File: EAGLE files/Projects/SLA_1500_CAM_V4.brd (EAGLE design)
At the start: 37.8 x 26.4 mm, 88 parts, among them J2 JST GH SM06B, J3 MOLEX 53261-03, J4 MOLEX 53261-04, J5 MOLEX 53261-04, J6 MOLEX 53261-04, U11 TXS0102, U2 TPS73633DCQR, U8 TXS0102, U9 TXS0102

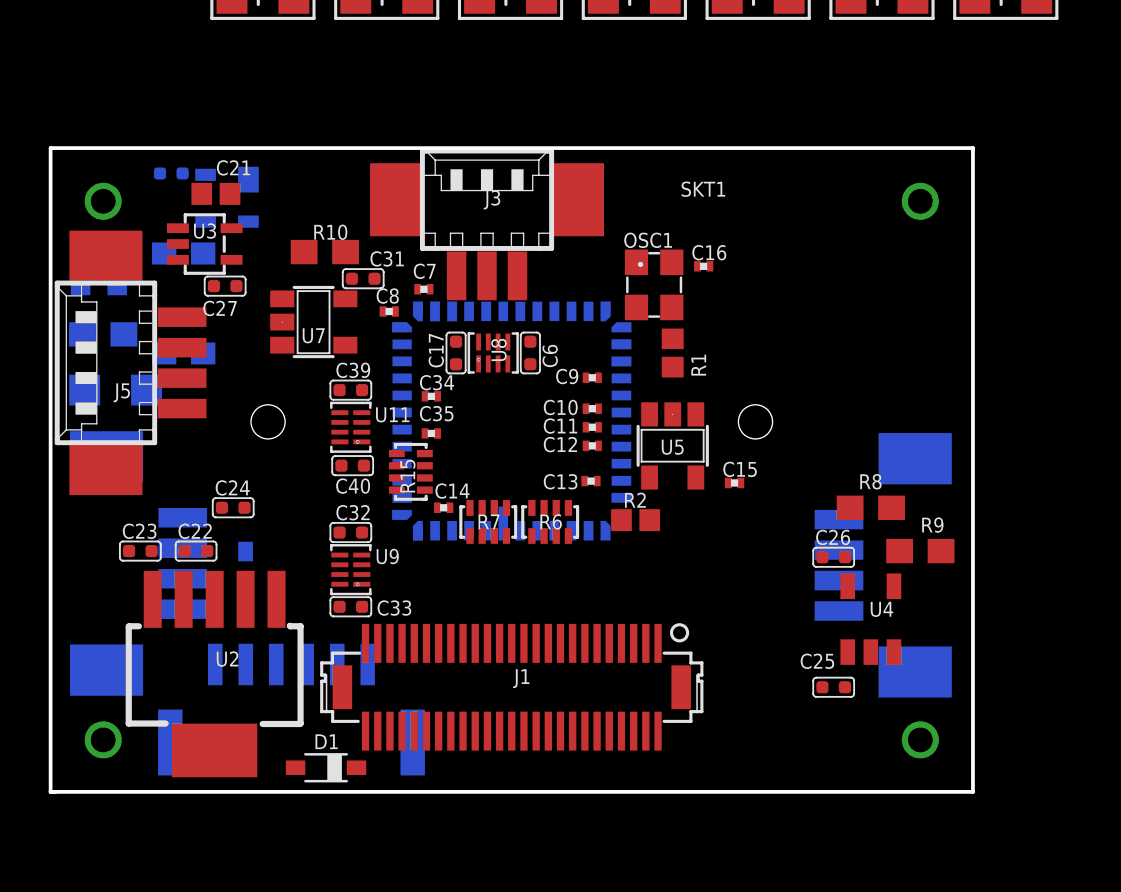
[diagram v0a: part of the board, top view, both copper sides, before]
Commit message: Update SLA1500 CAM V4
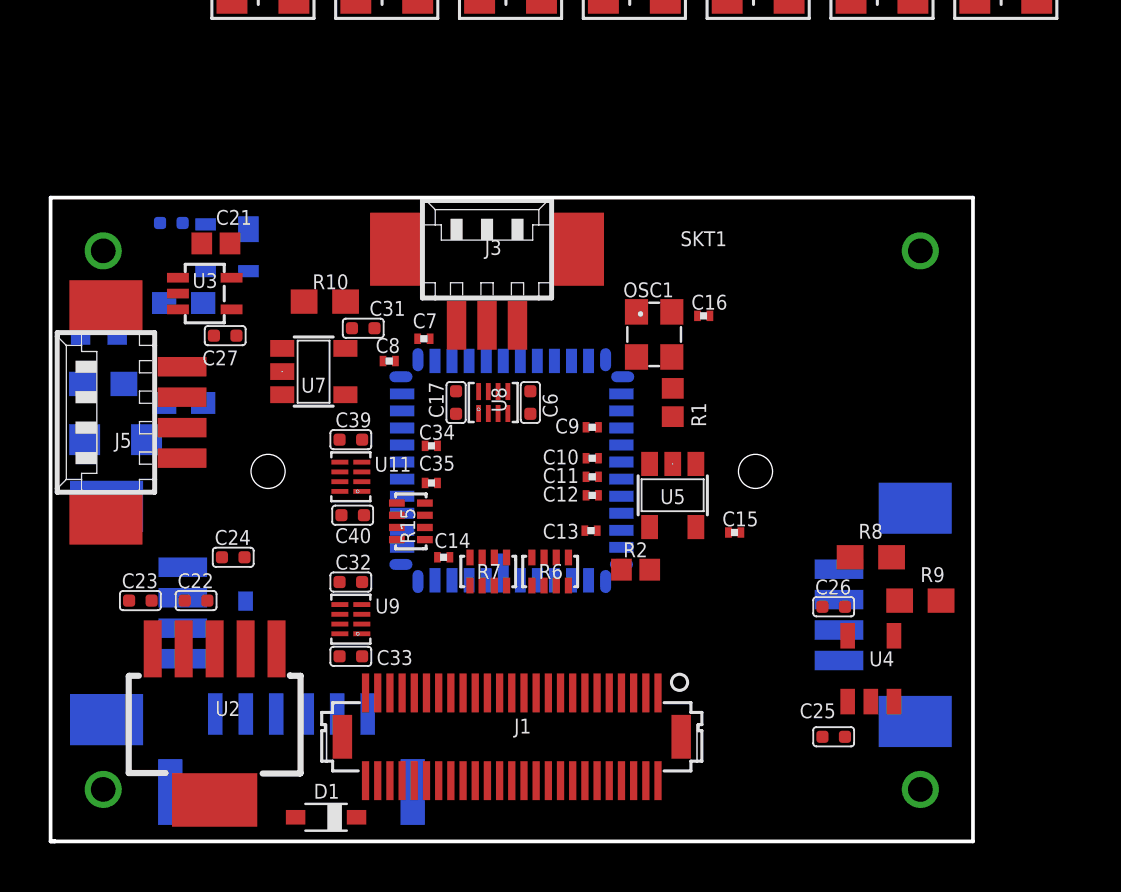
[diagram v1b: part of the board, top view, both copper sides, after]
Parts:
- U1: device Sightline:ILCC48 -> Sightline:ILCC48_KD
- moved R10 2.03 mm to (-7.67, 6.93)
- moved C10 2.03 mm to (3.30, 0.51)
- moved C11 2.03 mm to (3.30, -0.25)
- moved C12 2.03 mm to (3.30, -1.02)
- moved C13 2.03 mm to (3.25, -2.46)
- moved C14 2.03 mm to (-2.79, -3.56)
- moved C15 2.03 mm to (9.14, -2.54)
- moved C16 2.03 mm to (7.87, 6.35)
- moved C21 2.03 mm to (-12.1, 9.32)
- moved C24 2.03 mm to (-11.4, -3.56)
- moved C25 2.03 mm to (13.2, -10.9)
- moved C26 2.03 mm to (13.2, -5.59)
- moved C27 2.03 mm to (-11.8, 5.54)
- moved C30 2.03 mm to (-14.0, 10.2)
- moved C31 2.03 mm to (-6.10, 5.84)
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
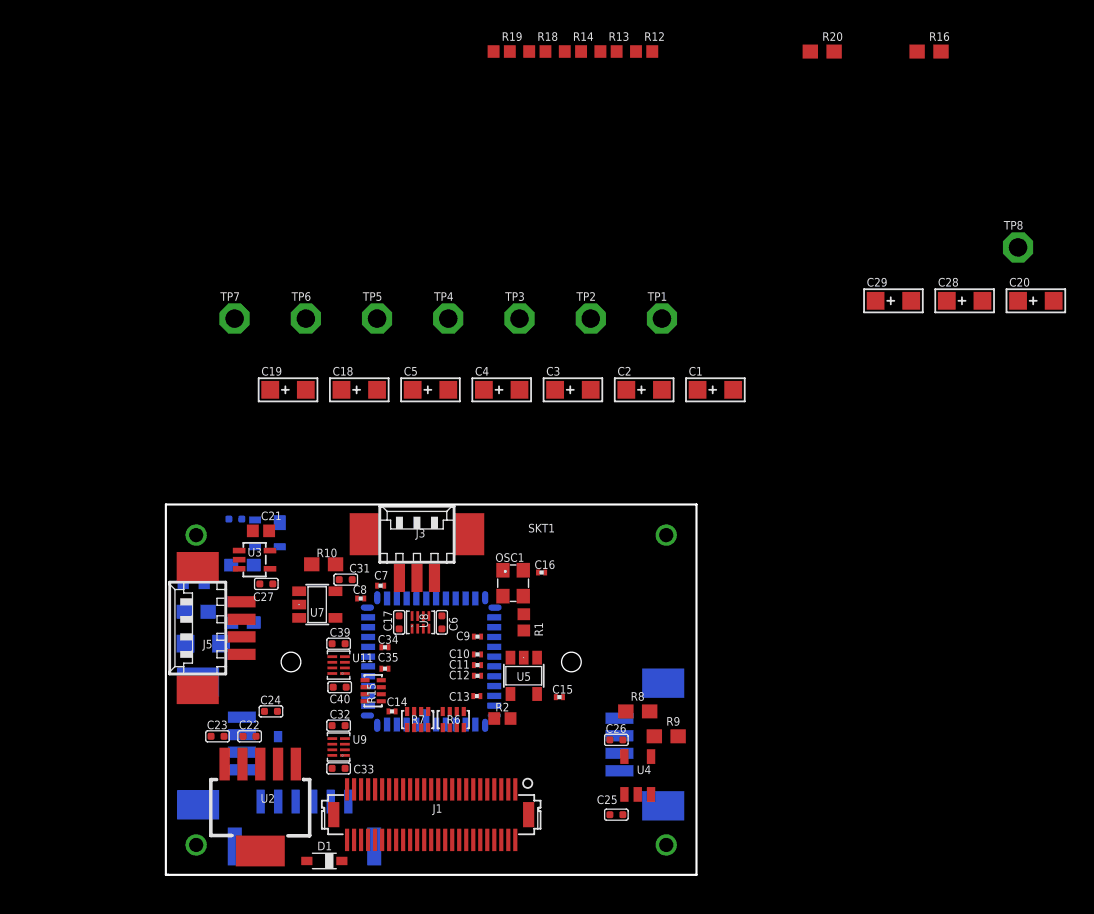
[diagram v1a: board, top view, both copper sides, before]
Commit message: Update SLA1500 CAM V4
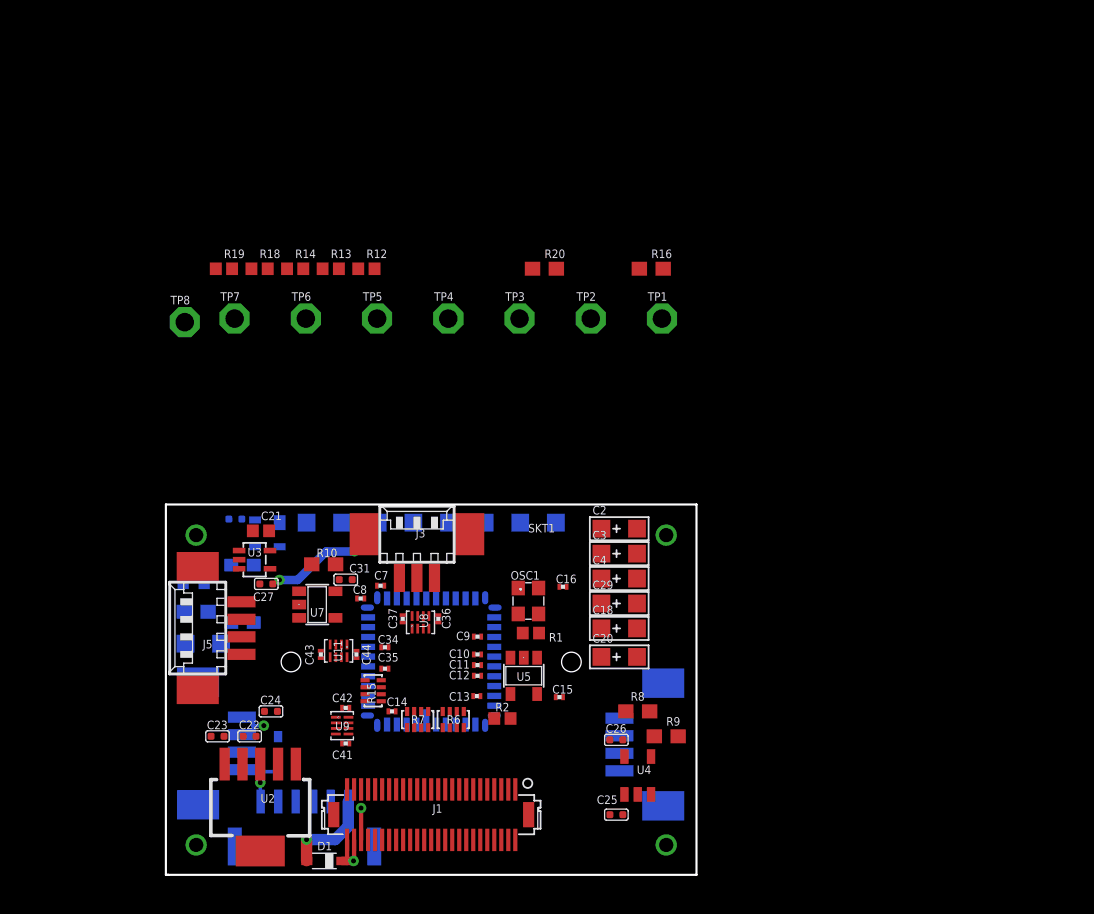
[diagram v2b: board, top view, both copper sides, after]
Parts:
- removed C17, C32, C33, C39, C40, C6: 100nf, Seeed-Capacitor:C0402
- added C36, C37, C41, C42, C43, C44: (no value), Sightline:R0201
- moved TP8 59.7 mm to (-17.6, 24.2)
- moved C28 43.6 mm to (-2.54, 9.91), flipped to the bottom, turned to 180 degrees
- moved C20 39.1 mm to (13.4, 0.33)
- moved C1 29.5 mm to (-7.62, 9.91), flipped to the bottom
- moved C29 29.1 mm to (13.4, 4.14)
- moved C18 25.2 mm to (13.4, 2.36)
- moved R13 25.2 mm to (-7.16, 28.0)
- moved R18 25.2 mm to (-12.2, 28.0)
- moved R19 25.2 mm to (-14.8, 28.0)
- moved R12 25.2 mm to (-4.62, 28.0)
- moved R14 25.2 mm to (-9.70, 28.0)
- moved R16 25.2 mm to (15.7, 28.0)
- moved R20 25.2 mm to (8.08, 28.0)
- moved C19 15.9 mm to (2.54, 9.91), flipped to the bottom
- moved C4 15.9 mm to (13.4, 5.92)
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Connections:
- net GND: now also C36.2, C37.2, C41.2, C42.2, C43.2, C44.2; no longer C17.2, C32.1, C33.2, C39.1, C40.2, C6.1
- net P1P8V: now also C36.1, C41.1, C43.1; no longer C32.2, C39.2, C6.2
- net P3P3V: now also C37.1, C42.1, C44.1; no longer C17.1, C33.1, C40.1
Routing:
- net N$34: track 0.00 -> 6.67 mm, vias 0 -> 1
- net N$2: track 0.00 -> 6.21 mm, vias 0 -> 2
- net N$39: track 0.00 -> 5.47 mm
- net GND: track 0.00 -> 4.94 mm, vias 0 -> 2
- net P5V: track 0.00 -> 3.85 mm, vias 0 -> 1
- net P1P8V: track 0.00 -> 2.27 mm, vias 0 -> 1
- added copper zone on layer 15, net GND
- added copper zone on layer 2, net P1P8V
- added copper zone on layer 2, net P2P8V
- added copper zone on layer 2, net P3P3V
- added copper zone on layer 2, net P5V

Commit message: Update SLA1500 CAM
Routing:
- net P5V: track 3.85 -> 2.87 mm
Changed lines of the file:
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@@
 </polygon>
 <wire x1="-12.7" y1="-5.217" x2="-13.502" y2="-5.217" width="0.254" layer="16"/>
-<wire x1="-12.164" y1="-9.988" x2="-12.192" y2="-9.988" width="0.254" layer="16"/>
-<wire x1="-12.192" y1="-9.988" x2="-12.192" y2="-8.636" width="0.254" layer="16"/>
-<via x="-12.192" y="-8.636" extent="15-16" drill="0.35"/>
+<wire x1="-12.164" y1="-9.988" x2="-12.1666" y2="-9.988" width="0.254" layer="16"/>
+<wire x1="-12.1666" y1="-9.988" x2="-12.1666" y2="-8.5344" width="0.254" layer="16"/>
+<via x="-12.1666" y="-8.5344" extent="15-16" drill="0.35"/>
 <wire x1="-13.502" y1="-3.967" x2="-12.797" y2="-3.967" width="0.254" layer="16"/>
 <wire x1="-12.797" y1="-3.967" x2="-12.7" y2="-4.064" width="0.254" layer="16"/>
@@
 <wire x1="-11.8925" y1="-3.556" x2="-12.7" y2="-4.064" width="0" layer="19" extent="1-16"/>
 <wire x1="-14.7775" y1="-5.334" x2="-13.502" y2="-5.217" width="0" layer="19" extent="1-16"/>
-<wire x1="-12.192" y1="-7.314" x2="-12.192" y2="-8.636" width="0" layer="19" extent="1-16"/>
+<wire x1="-12.192" y1="-7.314" x2="-12.1666" y2="-8.5344" width="0" layer="19" extent="1-16"/>
 <wire x1="14.6812" y1="9.4742" x2="16.764" y2="9.017" width="0" layer="19" extent="1-1"/>
 <wire x1="14.6812" y1="7.6962" x2="14.6812" y2="9.4742" width="0" layer="19" extent="1-1"/>
@@
 <vertex x="-19.0754" y="6.096"/>
 </polygon>
-<wire x1="-6.37" y1="-14.224" x2="-5.9944" y2="-14.224" width="0.6096" layer="1"/>
-<via x="-5.5372" y="-14.224" extent="1-2" drill="0.35"/>
-<wire x1="-5.9944" y1="-14.224" x2="-5.5372" y2="-14.224" width="0.6096" layer="1"/>
-<wire x1="-6" y1="-12.722" x2="-6" y2="-14.2184" width="0.3048" layer="1"/>
-<wire x1="-6" y1="-14.2184" x2="-5.9944" y2="-14.224" width="0.3048" layer="1"/>
-<wire x1="-5.5" y1="-12.722" x2="-5.5" y2="-14.1868" width="0.3048" layer="1"/>
-<wire x1="-5.5" y1="-14.1868" x2="-5.5372" y2="-14.224" width="0.3048" layer="1"/>
+<wire x1="-5.5" y1="-12.722" x2="-6" y2="-12.722" width="0.3048" layer="1"/>
+<wire x1="-6.37" y1="-14.224" x2="-5.5118" y2="-14.224" width="0.508" layer="1"/>
+<via x="-5.5118" y="-14.224" extent="1-2" drill="0.35"/>
+<wire x1="-5.5" y1="-12.722" x2="-5.5" y2="-14.2122" width="0.3048" layer="1"/>
+<wire x1="-5.5" y1="-14.2122" x2="-5.5118" y2="-14.224" width="0.3048" layer="1"/>
 <wire x1="-17.614" y1="3.556" x2="1.2192" y2="24.4602" width="0" layer="19" extent="16-16"/>
 <wire x1="-17.526" y1="1.27" x2="-17.614" y2="3.556" width="0" layer="19" extent="16-16"/>

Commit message: Update SLA1500 CAM V4 .brd
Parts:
- moved LED1 1.78 mm to (-15.2, 5.41), turned to 90 degrees
- moved C22 1.50 mm to (-13.9, -4.19)
- moved C23 1.15 mm to (-16.4, -5.26), turned to 90 degrees
- moved C30 1.04 mm to (-14.4, 9.19)
- moved R2 0.15 mm to (5.08, -4.22)
- moved U6 0.08 mm to (-11.7, 9.22)
- moved U5 0.05 mm to (6.60, -1.07)
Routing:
- net GND: track 5.02 -> 53.3 mm, vias 2 -> 8
- net P3P3V: track 0.00 -> 17.1 mm, vias 0 -> 4
- net P5V: track 2.87 -> 16.2 mm, vias 1 -> 6
- net N$2: track 6.21 -> 0.00 mm, vias 2 -> 0
- net N$27: track 0.00 -> 5.52 mm
- net N$30: track 0.00 -> 1.85 mm
- net N$39: track 5.47 -> 4.04 mm

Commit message: Update SLA1500 CAM V4 .brd
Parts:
- moved R16 50.7 mm to (-27.4, 1.27)
- moved R14 44.3 mm to (3.71, -14.2), flipped to the bottom, turned to 180 degrees
- moved R20 43.1 mm to (-27.3, 3.51)
- moved R12 42.2 mm to (-1.32, -14.1), flipped to the bottom
- moved R19 31.2 mm to (-7.72, -2.34), turned to 270 degrees
- moved R13 24.7 mm to (4.19, 6.12)
- moved R18 23.5 mm to (-3.61, 6.20), turned to 180 degrees
- moved TP1 23.3 mm to (-4.50, 14.2)
- moved TP4 21.7 mm to (-17.7, 13.8)
- moved TP2 13.2 mm to (3.15, 14.1)
- moved TP5 13.1 mm to (-12.6, 14.8)
- moved TP6 12.2 mm to (2.84, 21.5)
- moved TP8 11.8 mm to (-7.44, 18.2)
- moved TP3 7.72 mm to (2.57, 17.7)
- moved TP7 6.75 mm to (-11.5, 18.2)
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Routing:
- net GND: track 53.3 -> 3.10 mm, vias 8 -> 5
- net P1P8V: track 2.02 -> 36.7 mm, vias 1 -> 12
- net P2P8V: track 0.00 -> 27.8 mm, vias 0 -> 8
- net P5V: track 16.2 -> 27.8 mm, vias 6 -> 7
- net P3P3V: track 17.1 -> 24.1 mm, vias 4 -> 8
- net N$31: track 0.00 -> 3.73 mm, vias 0 -> 1
- net N$23: track 0.00 -> 3.28 mm
- net N$21: track 0.00 -> 3.13 mm
- net N$30: track 1.85 -> 4.04 mm
- net N$25: track 0.00 -> 1.85 mm
- net N$15: track 0.00 -> 1.84 mm
- net N$16: track 0.00 -> 1.37 mm
- added copper zone on layer 1, net GND
- added copper zone on layer 16, net GND
- added copper zone on layer 1, net P5V

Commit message: Update SLA1500 CAM V4 .brd
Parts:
- moved R14 23.2 mm to (10.3, 8.03), turned to 0 degrees
- moved J3 22.3 mm to (16.2, -7.16), turned to 270 degrees
- moved C37 15.1 mm to (10.0, -5.23), turned to 90 degrees
- moved C36 15.0 mm to (10.0, -8.15), turned to 270 degrees
- moved U8 14.4 mm to (9.60, -6.73), turned to 270 degrees
- moved C18 10.2 mm to (22.9, -1.45)
- moved C2 10.2 mm to (22.9, 5.66)
- moved C20 10.2 mm to (22.9, -3.48)
- moved C29 10.2 mm to (22.9, 0.33)
- moved C3 10.2 mm to (22.9, 3.89)
- moved C4 10.2 mm to (22.9, 2.11)
- moved C25 9.38 mm to (13.7, -1.50)
- moved C26 9.38 mm to (13.7, 3.86)
- moved R8 9.38 mm to (15.0, 5.79)
- moved R9 9.38 mm to (16.9, 3.99)
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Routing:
- net CAM_GPIO172: track 0.00 -> 44.5 mm, vias 0 -> 3
- net CAM_GPIO173: track 0.00 -> 35.3 mm, vias 0 -> 3
- net CAM_GPIO178: track 0.00 -> 22.2 mm, vias 0 -> 1
- net N$33: track 0.00 -> 11.4 mm
- net N$53: track 0.00 -> 10.7 mm
- net N$32: track 0.00 -> 7.42 mm, vias 0 -> 1
- net N$1: track 0.00 -> 6.45 mm, vias 0 -> 1
- net N$17: track 0.00 -> 5.20 mm, vias 0 -> 1
- net PIXCLK: track 0.00 -> 4.64 mm, vias 0 -> 1
- net P1P8V: track 36.7 -> 34.3 mm, vias 12 -> 10
- net P2P8V: track 27.8 -> 26.4 mm, vias 8 -> 7
- net P5V: track 27.8 -> 26.7 mm, vias 7 -> 6
- net P3P3V: track 24.1 -> 23.3 mm, vias 8 -> 7
- net N$31: track 3.73 -> 3.21 mm

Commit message: Update SLA1500 CAM V4 .brd
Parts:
- added R17, R21, R22, R23, R24, R25, R3, R4, R5: 22R, Seeed-Resistor:R0402
- R15, R6: value 33R -> 22R; device Sightline:DILR-4 -> Seeed-Resistor:R0402
- R7: value (none) -> 22R; device Sightline:DILR-4 -> Seeed-Resistor:R0402
- moved R15 5.52 mm to (-0.97, -6.60), turned to 0 degrees
- moved R6 2.65 mm to (0.66, -6.63), turned to 0 degrees
- moved R7 2.56 mm to (-0.25, -6.60), turned to 0 degrees
- moved C37 2.03 mm to (9.91, -7.26), turned to 180 degrees
- moved U8 1.87 mm to (9.86, -8.59)
- moved C36 1.71 mm to (9.88, -9.86), turned to 180 degrees
- moved C16 0.38 mm to (8.84, 4.85)
- moved C14 0.13 mm to (-2.03, -1.91)
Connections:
- removed net N$10 (its old number): R6.4, U1.48
- removed net N$50: R15.4, U1.11
- removed net N$51: J1.23, R15.5
- new net N$12: R15.1, U1.2
- new net N$2: R3.1, U1.45
- new net N$3: J1.36, R3.2
- net N$11: now also J1.32, R7.2; no longer J1.33, R6.5
- net N$14: now also J1.31, R15.2; no longer J1.32, R7.8
- net N$22: now also R17.1, U1.3; no longer R7.2, U1.2
- net N$24: now also J1.30, R17.2; no longer J1.31, R7.7
- net N$4: now also R4.1, U1.46; no longer R6.1, U1.45
- net N$40: now also R21.1, U1.7; no longer R7.3, U1.3
- net N$41: now also J1.29, R21.2; no longer J1.30, R7.6
- net N$42: now also R22.1, U1.8; no longer R7.4, U1.7
- net N$43: now also J1.26, R22.2; no longer J1.29, R7.5
- net N$44: now also R23.1, U1.9; no longer R15.1, U1.8
- net N$45: now also J1.25, R23.2; no longer J1.26, R15.8
- net N$46: now also R24.1, U1.10; no longer R15.2, U1.9
- net N$47: now also J1.24, R24.2; no longer J1.25, R15.7
- net N$48: now also R25.1, U1.11; no longer R15.3, U1.10
- net N$49: now also J1.23, R25.2; no longer J1.24, R15.6
- net N$5: now also J1.35, R4.2; no longer J1.36, R6.8
- net N$6: now also R5.1, U1.47; no longer R6.2, U1.46
- net N$7: now also J1.34, R5.2; no longer J1.35, R6.7
- net N$8: now also R6.1, U1.48; no longer R6.3, U1.47
- net N$9: now also J1.33, R6.2; no longer J1.34, R6.6
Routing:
- net FRAME_VALID: track 0.00 -> 27.9 mm, vias 0 -> 1
- net STANDBY: track 0.00 -> 27.6 mm, vias 0 -> 3
- net LINE_VALID: track 0.00 -> 22.6 mm, vias 0 -> 1
- net P1P8V: track 34.3 -> 43.0 mm, vias 10 -> 11
- net N$20: track 0.00 -> 8.53 mm
- net N$13: track 0.00 -> 5.32 mm
- net N$19: track 0.00 -> 4.54 mm
- net N$18: track 0.00 -> 4.51 mm
- net N$52: track 0.00 -> 3.97 mm, vias 0 -> 1
- net P2P8V: track 26.4 -> 22.8 mm, vias 7 -> 9
- net P5V: track 26.7 -> 29.8 mm, vias 6 -> 7
- net P3P3V: track 23.3 -> 25.1 mm, vias 7 -> 8

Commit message: Update SLA1500 CAM V4 .brd
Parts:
- removed R25: 22R, Seeed-Resistor:R0402
- removed U2: TPS73633DCQR, Sightline:SOT-223-6-PIN
- added R26: 33R, resistor:R0201
- added U10: TPS73633DBVR, Sightline:SOT23-5
- R15, R17, R21, R22, R23, R24, R3, R4, R5, R6, R7: value 22R -> 33R; device Seeed-Resistor:R0402 -> resistor:R0201
- moved R17 21.0 mm to (-22.6, -3.78), turned to 270 degrees
- moved C22 5.47 mm to (-14.1, -9.65)
- moved R24 3.53 mm to (-22.8, 1.50)
- moved D1 3.47 mm to (-8.69, -10.9), turned to 270 degrees
- moved R23 3.24 mm to (-22.4, 0.18)
- moved C24 3.09 mm to (-14.1, -5.03)
- moved R4 3.04 mm to (1.04, -9.32), flipped to the bottom, turned to 270 degrees
- moved R22 2.94 mm to (-22.5, -1.14)
- moved R6 2.88 mm to (-0.36, -9.32), flipped to the bottom, turned to 270 degrees
- moved R15 2.83 mm to (-1.75, -9.32), flipped to the bottom, turned to 270 degrees
- moved R21 2.66 mm to (-22.7, -2.46)
- moved R3 2.59 mm to (0.76, -5.99), turned to 180 degrees
- moved C7 2.05 mm to (-3.68, 6.35), turned to 0 degrees
- moved R5 1.89 mm to (-0.33, -6.40), turned to 180 degrees
- moved R7 1.50 mm to (-1.22, -7.75), turned to 180 degrees
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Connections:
- net GND: now also U10.2; no longer U2.3, U2.6
- net N$10: now also R6.1; no longer R7.1
- net N$11: now also R6.2; no longer R7.2
- net N$12: now also R7.1; no longer R15.1
- net N$14: now also R7.2; no longer R15.2
- net N$2: now also R26.1; no longer R3.1
- net N$21: now also U10.4; no longer U2.4
- net N$22: now also R15.1; no longer R17.1
- net N$24: now also R15.2; no longer R17.2
- net N$3: now also R26.2; no longer R3.2
- net N$4: now also R3.1; no longer R4.1
- net N$40: now also R17.1; no longer R21.1
- net N$41: now also R17.2; no longer R21.2
- net N$42: now also R21.1; no longer R22.1
- net N$43: now also R21.2; no longer R22.2
- net N$44: now also R22.1; no longer R23.1
- net N$45: now also R22.2; no longer R23.2
- net N$46: now also R23.1; no longer R24.1
- net N$47: now also R23.2; no longer R24.2
- net N$48: now also R24.1; no longer R25.1
- net N$49: now also R24.2; no longer R25.2
- net N$5: now also R3.2; no longer R4.2
- net N$6: now also R4.1; no longer R5.1
- net N$7: now also R4.2; no longer R5.2
- net N$8: now also R5.1; no longer R6.1
- net N$9: now also R5.2; no longer R6.2
- net P3P3V: now also U10.5; no longer U2.2
- net P5V: now also U10.1, U10.3; no longer U2.1, U2.5
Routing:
- net I2C_SDA: track 0.00 -> 41.1 mm, vias 0 -> 3
- net I2C_SCL: track 0.00 -> 21.8 mm, vias 0 -> 3
- net CAM_GPIO173: track 35.3 -> 45.6 mm, vias 3 -> 4
- net N$26: track 0.00 -> 8.92 mm, vias 0 -> 1
- net CAM_GPIO172: track 44.5 -> 52.0 mm, vias 3 -> 4
- net P5V: track 29.8 -> 22.3 mm, vias 7 -> 9
- net N$5: track 0.00 -> 6.09 mm
- net N$2: track 0.00 -> 4.57 mm
- net N$6: track 0.00 -> 4.57 mm
- net N$22: track 0.00 -> 4.57 mm
- net N$9: track 0.00 -> 3.80 mm
- net N$8: track 0.00 -> 3.62 mm, vias 0 -> 1
- net N$12: track 0.00 -> 3.28 mm, vias 0 -> 1
- net N$4: track 0.00 -> 2.59 mm, vias 0 -> 1
- net P1P8V: track 43.0 -> 45.2 mm, vias 11 -> 12
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- removed copper zone on layer 1, net P5V
